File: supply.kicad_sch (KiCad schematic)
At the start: 24 parts, among them IC3 BQ25622ERYKR, IC4 BQ27427YZFR, IC7 TPS62291DRVR, IC8 TPS62293DRVR, J5 Conn_01x02

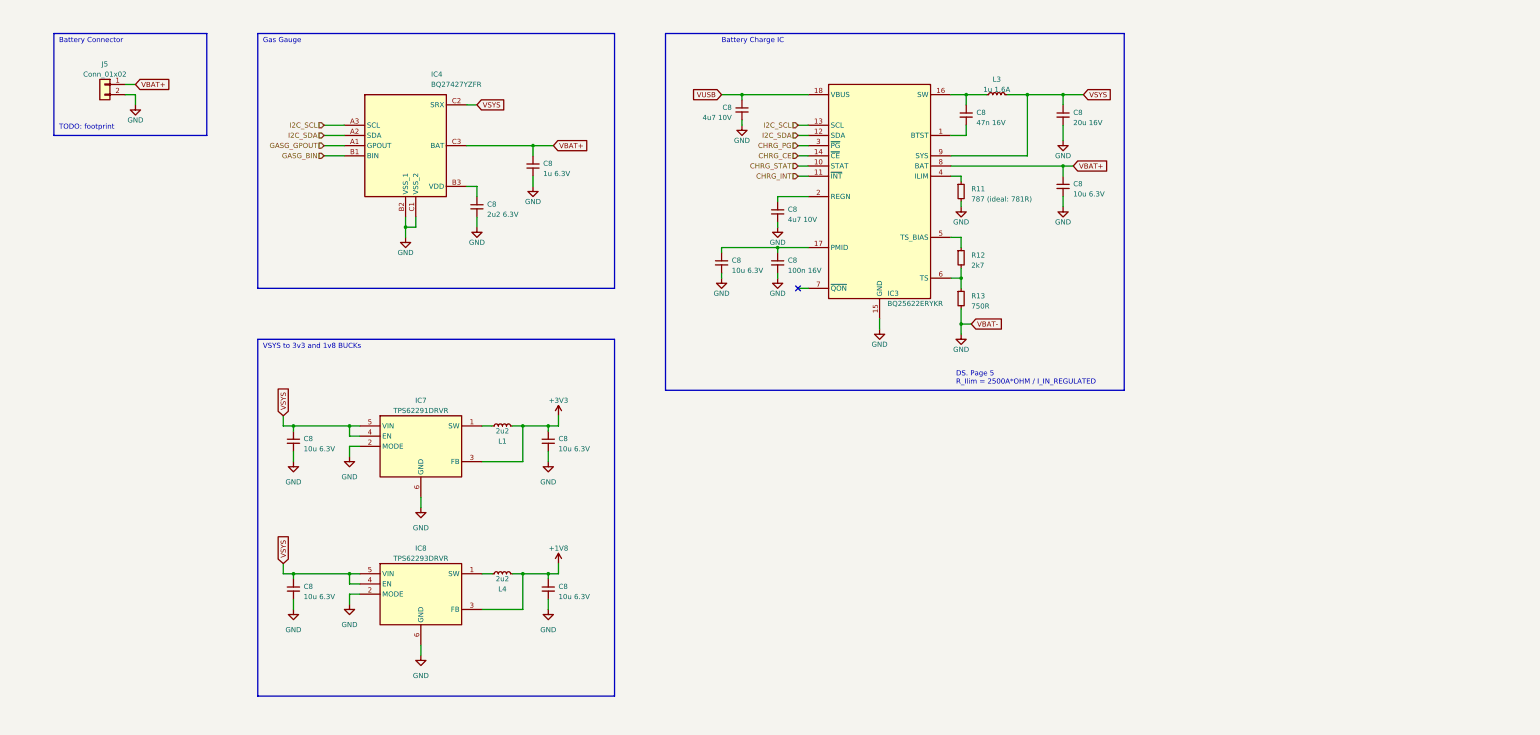
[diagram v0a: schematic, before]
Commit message: switched to other charge + protection IC
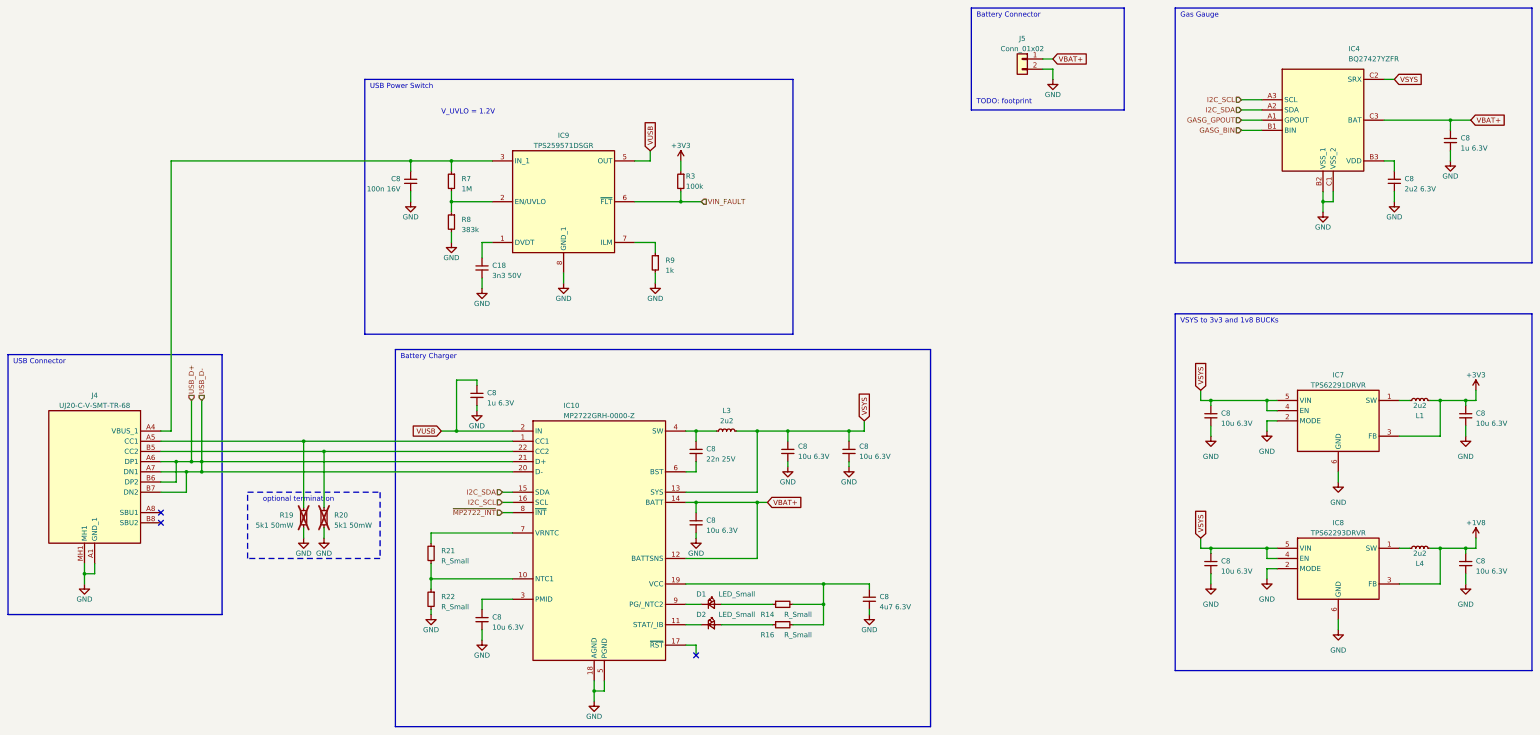
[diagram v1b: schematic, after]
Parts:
- removed C8: 20u 16V, ARMband:C_0704, symbol Device:C_Small
- removed C8: 100n 16V, Capacitor_SMD:C_0402_1005Metric, symbol Device:C_Small
- removed C8: 47n 16V, Capacitor_SMD:C_0201_0603Metric, symbol Device:C_Small
- removed C8 (x2): 4u7 10V, Capacitor_SMD:C_0402_1005Metric, symbol Device:C_Small
- removed C8 (x2): 10u 6.3V, Capacitor_SMD:C_0402_1005Metric, symbol Device:C_Small
- removed IC3: BQ25622ERYKR, ARMband:BQ25620RYKR, symbol ARMband:BQ25622ERYKR
- removed R11: 787 (ideal: 781R), Resistor_SMD:R_0201_0603Metric, symbol Device:R_Small
- removed R12: 2k7, symbol Device:R_Small
- removed R13: 750R, symbol Device:R_Small
- added C18: 3n3 50V, Capacitor_SMD:C_0402_1005Metric, symbol Device:C_Small
- added C8 (x4): 10u 6.3V, Capacitor_SMD:C_0402_1005Metric, symbol Device:C_Small
- added C8: 22n 25V, Capacitor_SMD:C_0402_1005Metric, symbol Device:C_Small
- added C8: 4u7 6.3V, Capacitor_SMD:C_0402_1005Metric, symbol Device:C_Small
- added C8: 100n 16V, Capacitor_SMD:C_0402_1005Metric, symbol Device:C_Small
- added C8: 1u 6.3V, Capacitor_SMD:C_0201_0603Metric, symbol Device:C_Small
- added D1, D2: LED_Small, symbol Device:LED_Small
- added IC10: MP2722GRH-0000-Z, ARMband:MP2722GRH0000Z, symbol ARMband:MP2722GRH-0000-Z
- added IC9: TPS259571DSGR, SON50P200X200X80-9N, symbol LibraryLoader:TPS259571DSGR
- added J4: UJ20-C-V-SMT-TR-68, ARMband:UJ20CVSMTTR68, symbol ARMband:UJ20-C-V-SMT-TR-68
- added R14, R16, R21, R22: R_Small, symbol Device:R_Small
- added R19, R20: 5k1 50mW, Resistor_SMD:R_0201_0603Metric, symbol Device:R_Small
- added R3: 100k, Resistor_SMD:R_0201_0603Metric_Pad0.64x0.40mm_HandSolder, symbol Device:R_Small
- added R7: 1M, Resistor_SMD:R_0201_0603Metric, symbol Device:R_Small
- added R8: 383k, Resistor_SMD:R_0201_0603Metric, symbol Device:R_Small
- added R9: 1k, Resistor_SMD:R_0201_0603Metric, symbol Device:R_Small
- L3: value 1u 1.6A -> 2u2; footprint Inductor_SMD:L_0603_1608Metric -> ARMband:INDC3225X120N; MFN 81-DFE18SAN1R0ME0L -> 652-SRP3212A-2R2M
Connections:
- net +3V3: now also R3.1
- net EP: now also C18.2, C8.2, C8.2, C8.2, C8.2, C8.2, C8.2, C8.2, IC10.18 (AGND), IC10.5 (PGND), IC9.8 (GND_1), IC9.9 (GND_2), J4.A1 (GND_1), J4.A12 (GND_2), J4.B1 (GND_3), J4.MH1, J4.MH2, J4.MH3, J4.MH4, R19.2, R20.2, R22.2, R8.2, R9.2
- net I2C_SCL: now also IC10.16 (SCL)
- net I2C_SDA: now also IC10.15 (SDA)
- net VBAT+: now also C8.1, IC10.12 (BATTSNS), IC10.14 (BATT)
- net VSYS: now also C8.1, C8.1, IC10.13 (SYS)
- net VUSB: now also C8.1, IC10.2 (IN), IC9.5 (OUT)
- net at L3.1: now also C8.1, IC10.4 (SW)
- new net: C18.1, IC9.1 (DVDT)
- new net: IC9.2 (EN/UVLO), R7.2, R8.1
- new net: C8.1, IC9.3 (IN_1), IC9.4 (IN_2), J4.A4 (VBUS_1), J4.A9 (VBUS_2), J4.B4 (VBUS_3), J4.B9 (VBUS_4), R7.1
- new net: IC9.7 (ILM), R9.1
- new net: IC10.10 (NTC1), R21.2, R22.1
- new net: IC10.22 (CC2), J4.B5 (CC2), R20.1
- new net: IC10.1 (CC1), J4.A5 (CC1), R19.1
- new net: C8.2, IC10.6 (BST)
- new net: C8.1, IC10.19 (VCC), R14.2, R16.2
- new net: IC10.7 (VRNTC), R21.1
- new net: D2.1 (K), IC10.11 (STAT/_IB)
- new net: C8.1, IC10.3 (PMID)
- new net: D1.1 (K), IC10.9 (PG/_NTC2)
- new net: D1.2 (A), R14.1
- new net: D2.2 (A), R16.1
- new net USB_D+: IC10.20 (D-), IC10.21 (D+), J4.A6 (DP1), J4.A7 (DN1), J4.B6 (DP2), J4.B7 (DN2)
- new net VIN_FAULT: IC9.6 (~{FLT}), R3.2
- new net ~{MP2722_INT}: IC10.8 (~{INT})
- no-connect marks 1 -> 3
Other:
- note added: "Battery Charger"
- note added: "USB Connector"
- note added: "USB Power Switch"
- note added: "V_UVLO = 1.2V"
- note added: "optional termination"
- note removed: "Battery Charge IC"
- note removed: "DS. Page 5 R_Ilim = 2500A*OHM / I_IN_REGULATED"
- moved on the sheet: C8, IC4, IC7, IC8, J5, L1, L4

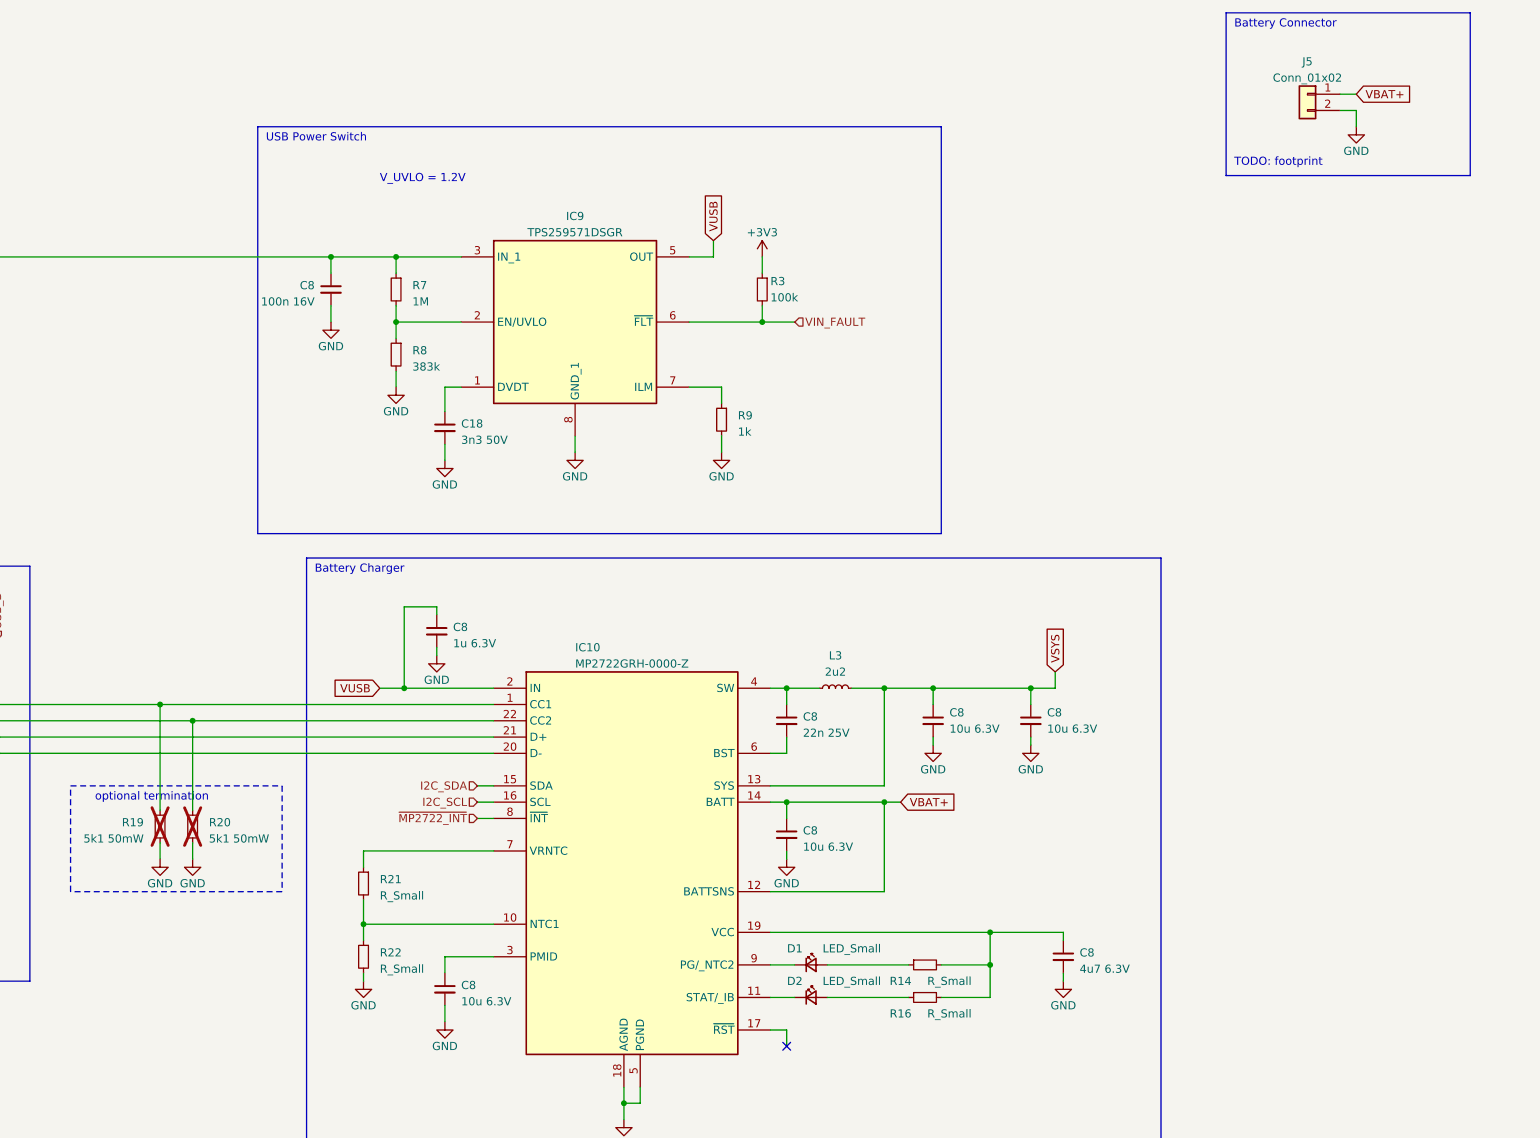
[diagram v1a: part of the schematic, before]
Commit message: Update resistors + LED values
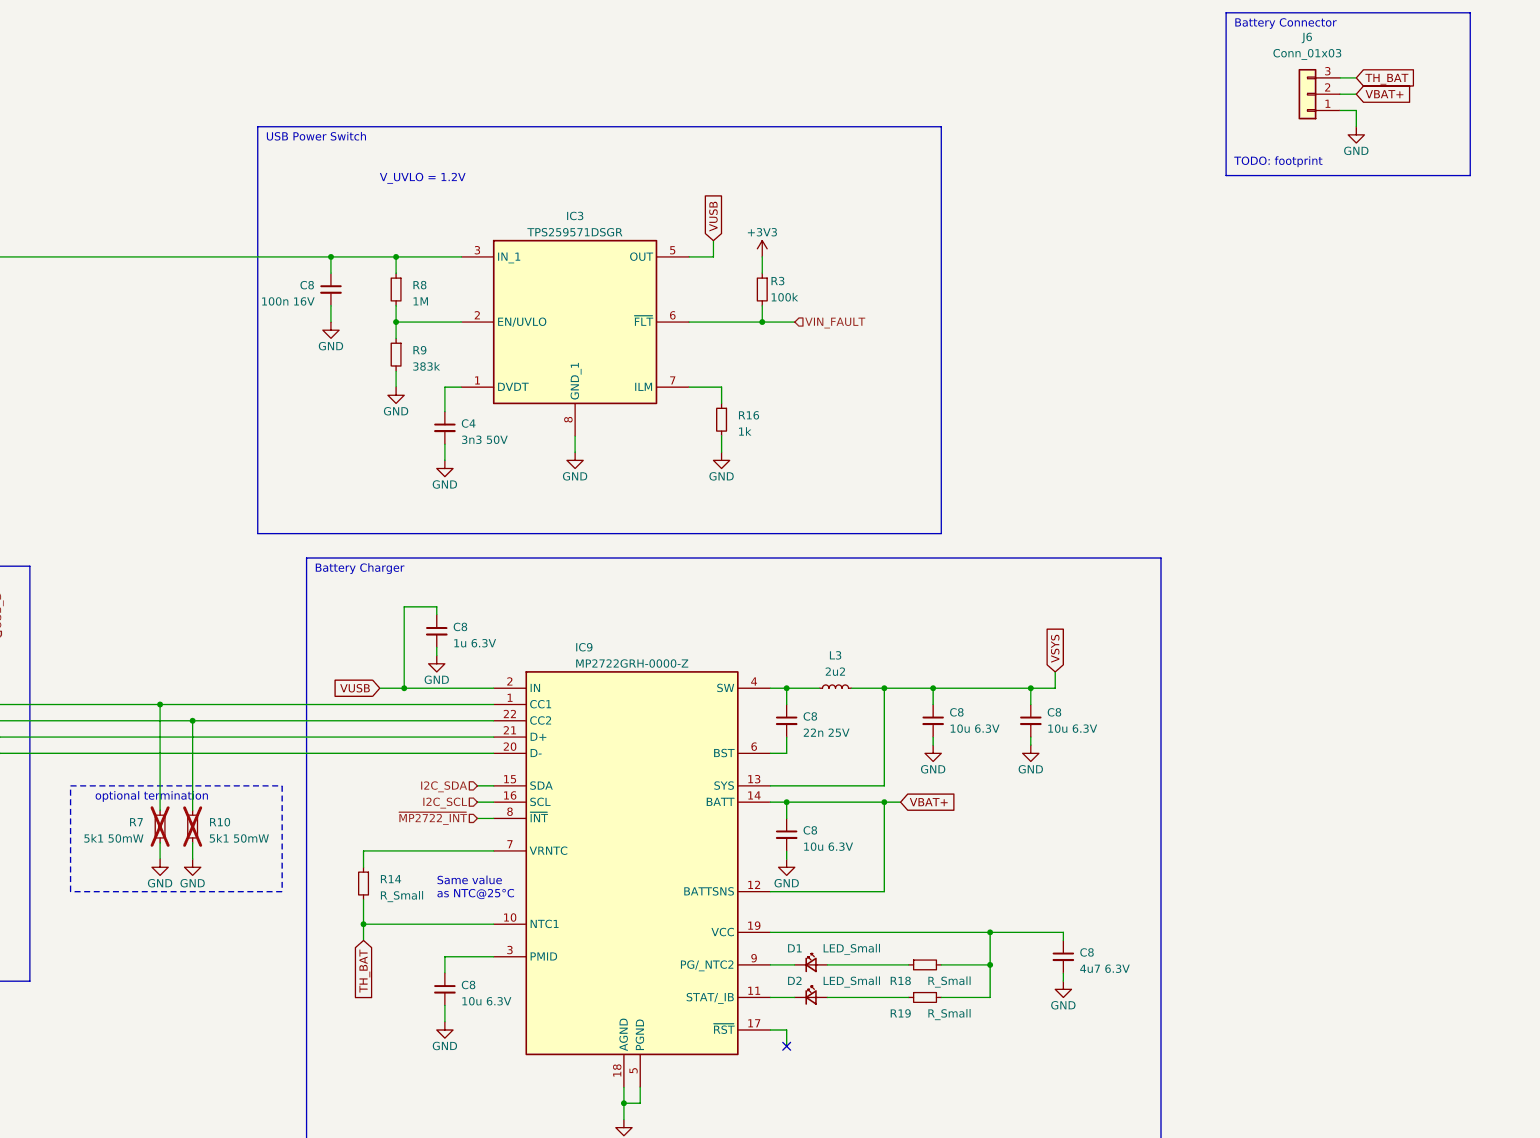
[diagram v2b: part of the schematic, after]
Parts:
- removed J5: Conn_01x02, symbol Connector_Generic:Conn_01x02
- removed R22: R_Small, symbol Device:R_Small
- added J6: Conn_01x03, symbol Connector_Generic:Conn_01x03
- renumbered C18 to C4, IC9 to IC3, IC10 to IC9, R20 to R10, R21 to R14, R9 to R16, R14 to R18, R16 to R19, R19 to R7, R7 to R8, R8 to R9
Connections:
- net EP: now also J6.1 (Pin_1)
- net VBAT+: now also J6.2 (Pin_2)
- net TH_BAT: now reaches IC9.10 (NTC1), R14.2
- net TH_BAT: now also J6.3 (Pin_3)
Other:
- note added: "Same value as NTC@25°C"

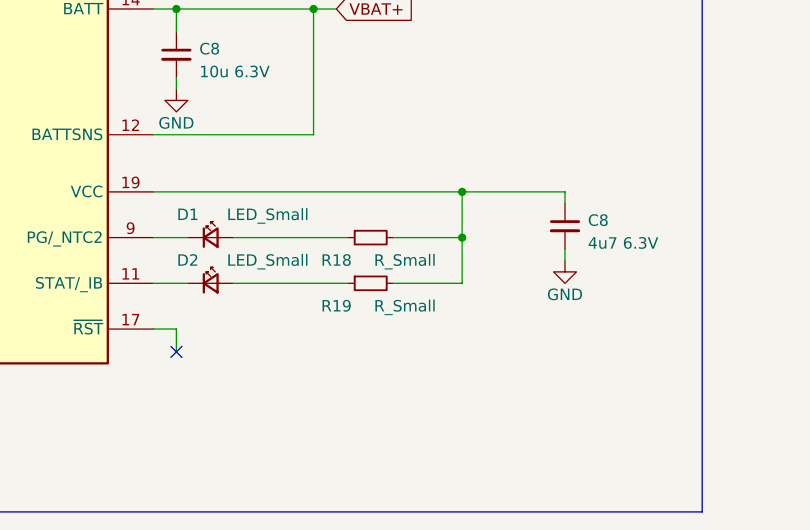
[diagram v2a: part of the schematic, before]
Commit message: Add MNR for LED
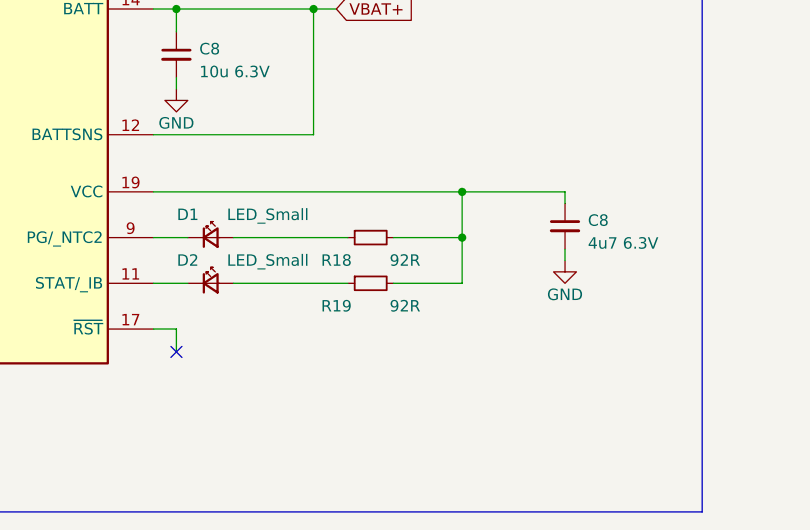
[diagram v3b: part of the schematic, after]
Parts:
- D1, D2: MNR (none) -> 755-SML-P12YTT86RR
- R18, R19: value R_Small -> 92R
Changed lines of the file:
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@@
       (effects (font (size 1.27 1.27)))
     )
-    (property "Value" "R_Small" (at 210.82 170.18 90)
+    (property "Value" "92R" (at 210.82 170.18 90)
       (effects (font (size 1.27 1.27)))
     )
@@
       (effects (font (size 1.27 1.27)))
     )
-    (property "Value" "R_Small" (at 210.82 175.26 90)
+    (property "Value" "92R" (at 210.82 175.26 90)
       (effects (font (size 1.27 1.27)))
     )
@@
       (effects (font (size 1.27 1.27)) hide)
     )
-    (property "Datasheet" "~" (at 189.23 172.72 90)
+    (property "Datasheet" "https://www.mouser.de/datasheet/2/348/rohm_semiconductor_rohm-s-a0008001703-1-1758187.pdf" (at 189.23 172.72 90)
+      (effects (font (size 1.27 1.27)) hide)
+    )
+    (property "MNR" "755-SML-P12YTT86RR" (at 189.23 172.72 0)
       (effects (font (size 1.27 1.27)) hide)
     )
@@
       (effects (font (size 1.27 1.27)) hide)
     )
-    (property "Datasheet" "~" (at 189.23 167.64 90)
-      (effects (font (size 1.27 1.27)) hide)
-    )
+    (property "Datasheet" "https://www.mouser.de/datasheet/2/348/rohm_semiconductor_rohm-s-a0008001703-1-1758187.pdf" (at 189.23 167.64 90)
+      (effects (font (size 1.27 1.27)) hide)
+    )
+    (property "MNR" "755-SML-P12YTT86RR" (at 189.23 167.64 0)
+      (effects (font (size 1.27 1.27)) hide)
+    )

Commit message: added TVS diodes and cleaned up supply.kicad_sch
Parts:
- added IC5: TPD6E001RSERG4, ARMband:TPD6E001RSERG4, symbol ARMband:TPD6E001RSERG4
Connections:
- net EP: now also IC5.5 (GND)
- net USB_D+: now also IC5.3 (IO3); no longer IC9.20 (D-), J4.A7 (DN1), J4.B7 (DN2)
- net at C8.1, IC3.3 (IN_1), IC3.4 (IN_2)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: now also IC5.10 (VCC)
- net at IC9.22 (CC2), J4.B5 (CC2), R10.1: now also IC5.2 (IO2)
- net at IC9.1 (CC1), J4.A5 (CC1), R7.1: now also IC5.1 (IO1)
- new net: IC5.4 (N.C._1), IC5.9 (N.C._2)
- new net USB_D-: IC5.6 (IO4), IC9.20 (D-), J4.A7 (DN1), J4.B7 (DN2)
- no-connect marks 3 -> 5
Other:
- note added: "BATTERY CHARGER, GAS GAUGE AND CONNECTOR"
- note added: "BUCKS"
- note added: "INPUT AND PROTECTION"
- note added: "TVS Diodes"
- moved on the sheet: C4, C8, D1, D2, IC3, IC4, IC7, IC8, IC9, J4, J6, L1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
